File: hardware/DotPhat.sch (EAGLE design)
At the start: 32 parts, among them CN1 1X4-BIG, IC1 CAT24M010TS, J2 RASPBERRYPI-40-PIN-GPIO_PTH, J3 USB-MICROB, U1 ATMEGA328P-MU-QFN32, U2 TMP102, U3 ATSHA204-TSU, X3 S4B-ZR

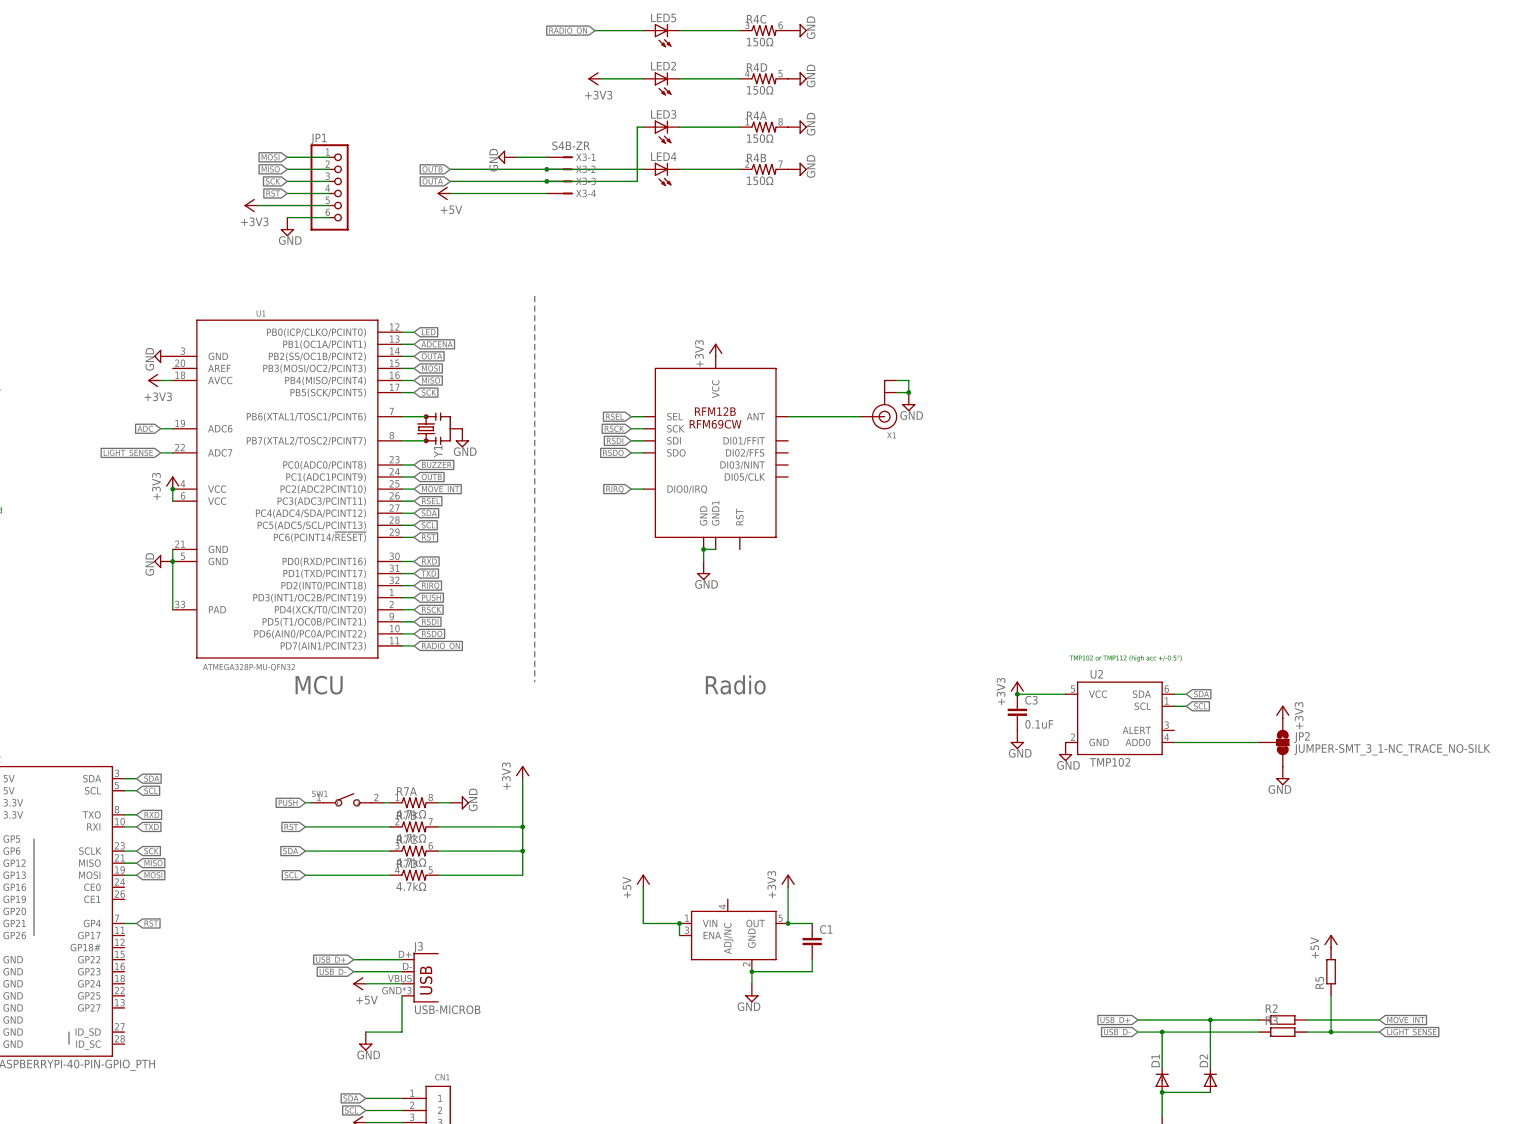
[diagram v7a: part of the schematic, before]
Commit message: Make USB_D+ and USB_D- part of the same port. Required for Micronucleus.
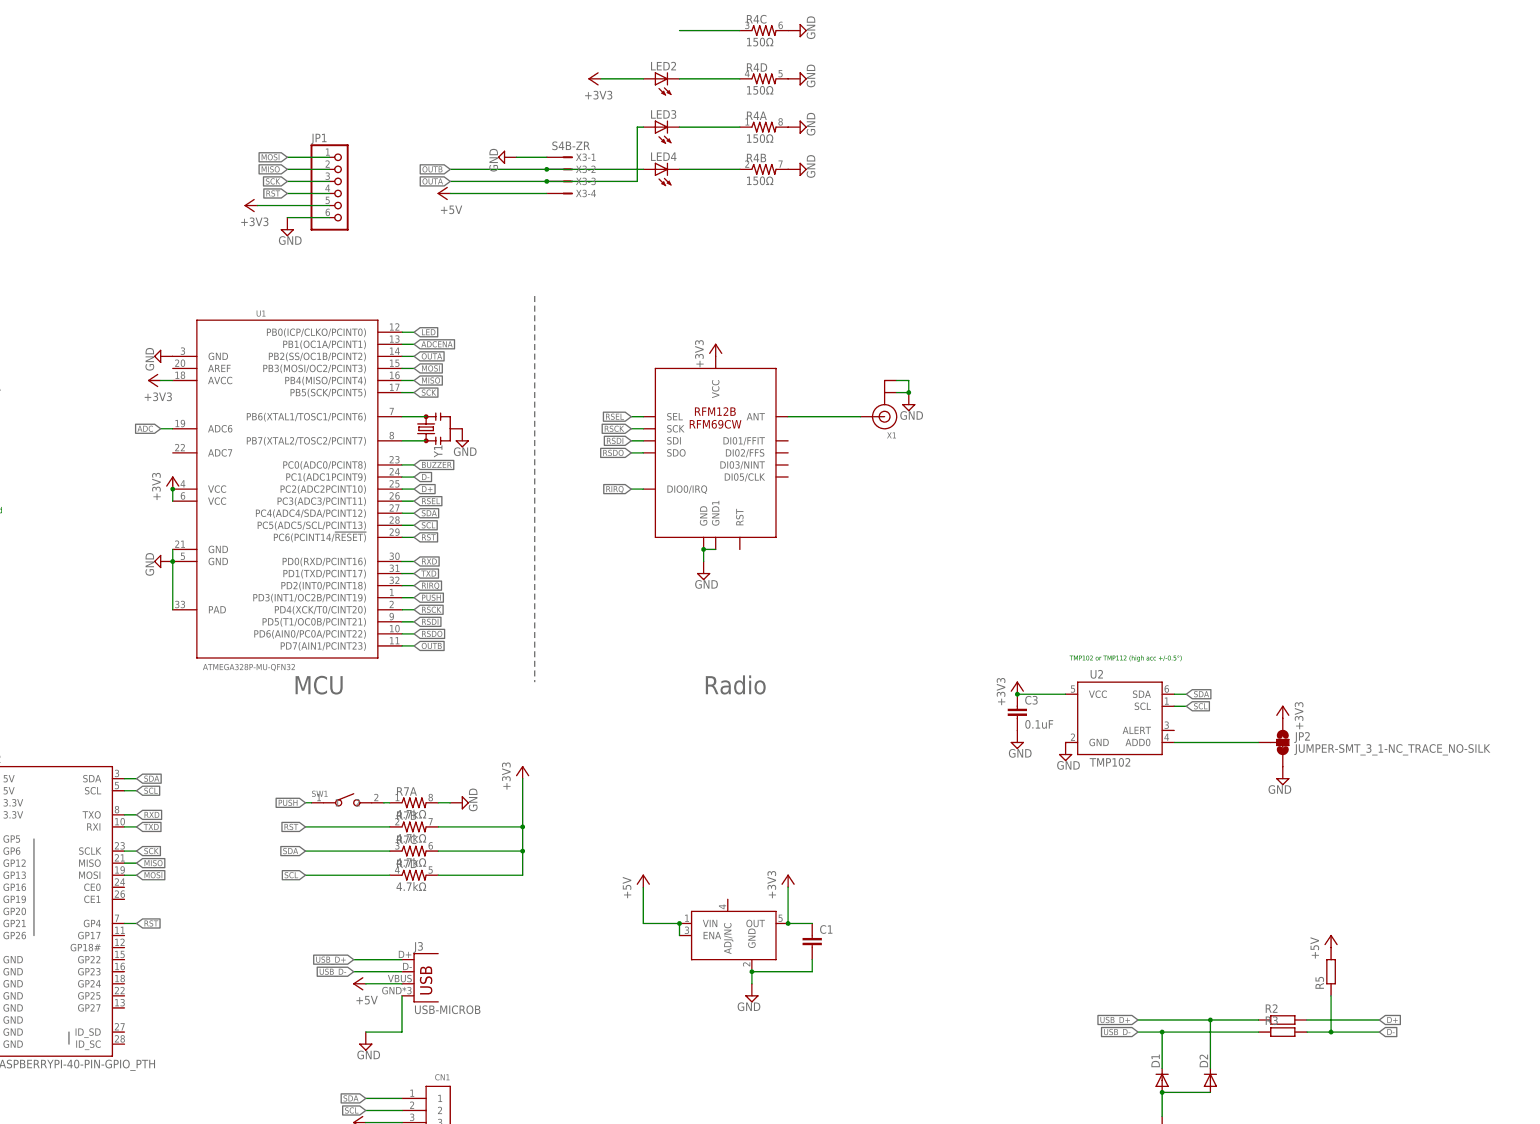
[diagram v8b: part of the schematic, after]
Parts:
- removed LED5: (no value), SparkFun:LED0603
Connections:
- net MOVE_INT renamed D+
- removed net LIGHT_SENSE: R3.2, R5.1, U1.ADC7
- removed net RADIO_ON: LED5.A, U1.PD7(AIN1/PCINT23)
- new net D-: R3.2, R5.1, U1.PC1(ADC1PCINT9)
- net N$10: no longer LED5.C
- net OUTB: now also U1.PD7(AIN1/PCINT23); no longer U1.PC1(ADC1PCINT9)
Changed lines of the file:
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@@
 <part name="+3V7" library="supply1" deviceset="+3V3" device=""/>
 <part name="R4" library="SparkFun" deviceset="RESISTOR-ARRAY" device="0603-ARV" value="150Ω"/>
-<part name="LED5" library="SparkFun" deviceset="LED" device="0603"/>
 <part name="SUPPLY12" library="supply2" deviceset="GND" device=""/>
 <part name="U$4" library="LDCL015" deviceset="LDCL015" device=""/>
@@
 <instance part="R4" gate="C" x="152.4" y="152.4"/>
 <instance part="R4" gate="D" x="152.4" y="142.24"/>
-<instance part="LED5" gate="G$1" x="129.54" y="152.4" rot="R90"/>
 <instance part="SUPPLY12" gate="GND" x="160.02" y="152.4" rot="R90"/>
 <instance part="U$4" gate="G$1" x="144.78" y="-38.1"/>
@@
 </segment>
 </net>
-<net name="LIGHT_SENSE" class="0">
-<segment>
-<pinref part="U1" gate="G$1" pin="ADC7"/>
-<wire x1="27.94" y1="63.5" x2="25.4" y2="63.5" width="0.1524" layer="91"/>
-<label x="25.4" y="63.5" size="1.27" layer="95" rot="R180" xref="yes"/>
-</segment>
-<segment>
-<pinref part="R3" gate="G$1" pin="2"/>
-<wire x1="266.7" y1="-58.42" x2="271.78" y2="-58.42" width="0.1524" layer="91"/>
-<pinref part="R5" gate="G$1" pin="1"/>
-<wire x1="271.78" y1="-58.42" x2="281.94" y2="-58.42" width="0.1524" layer="91"/>
-<wire x1="271.78" y1="-50.8" x2="271.78" y2="-58.42" width="0.1524" layer="91"/>
-<junction x="271.78" y="-58.42"/>
-<label x="281.94" y="-58.42" size="1.27" layer="95" xref="yes"/>
-</segment>
-</net>
 <net name="RSEL" class="0">
 <segment>
@@
 </segment>
 </net>
-<net name="MOVE_INT" class="0">
-<segment>
-<pinref part="U1" gate="G$1" pin="PC2(ADC2PCINT10)"/>
-<wire x1="76.2" y1="55.88" x2="78.74" y2="55.88" width="0.1524" layer="91"/>
-<label x="78.74" y="55.88" size="1.27" layer="95" xref="yes"/>
-</segment>
-<segment>
-<pinref part="R2" gate="G$1" pin="2"/>
-<wire x1="266.7" y1="-55.88" x2="281.94" y2="-55.88" width="0.1524" layer="91"/>
-<label x="281.94" y="-55.88" size="1.27" layer="95" xref="yes"/>
-</segment>
-</net>
 <net name="RXD" class="0">
 <segment>
@@
 </net>
 <net name="OUTB" class="0">
-<segment>
-<pinref part="U1" gate="G$1" pin="PC1(ADC1PCINT9)"/>
-<wire x1="76.2" y1="58.42" x2="78.74" y2="58.42" width="0.1524" layer="91"/>
-<label x="78.74" y="58.42" size="1.27" layer="95" xref="yes"/>
-</segment>
 <segment>
 <label x="86.36" y="123.19" size="1.27" layer="95" rot="R180" xref="yes"/>
@@
 <wire x1="106.68" y1="123.19" x2="127" y2="123.19" width="0.1524" layer="91"/>
 <junction x="106.68" y="123.19"/>
+</segment>
+<segment>
+<pinref part="U1" gate="G$1" pin="PD7(AIN1/PCINT23)"/>
+<wire x1="76.2" y1="22.86" x2="78.74" y2="22.86" width="0.1524" layer="91"/>
+<label x="78.74" y="22.86" size="1.27" layer="95" xref="yes"/>
 </segment>
 </net>
@@
 <segment>
 <pinref part="R4" gate="C" pin="1"/>
-<pinref part="LED5" gate="G$1" pin="C"/>
 <wire x1="147.32" y1="152.4" x2="134.62" y2="152.4" width="0.1524" layer="91"/>
-</segment>
-</net>
-<net name="RADIO_ON" class="0">
-<segment>
-<pinref part="LED5" gate="G$1" pin="A"/>
-<wire x1="127" y1="152.4" x2="116.84" y2="152.4" width="0.1524" layer="91"/>
-<label x="116.84" y="152.4" size="1.27" layer="95" rot="R180" xref="yes"/>
-</segment>
-<segment>
-<pinref part="U1" gate="G$1" pin="PD7(AIN1/PCINT23)"/>
-<wire x1="76.2" y1="22.86" x2="78.74" y2="22.86" width="0.1524" layer="91"/>
-<label x="78.74" y="22.86" size="1.27" layer="95" xref="yes"/>
 </segment>
 </net>
@@
 </segment>
 </net>
+<net name="D-" class="0">
+<segment>
+<pinref part="R3" gate="G$1" pin="2"/>
+<wire x1="266.7" y1="-58.42" x2="271.78" y2="-58.42" width="0.1524" layer="91"/>
+<pinref part="R5" gate="G$1" pin="1"/>
+<wire x1="271.78" y1="-58.42" x2="281.94" y2="-58.42" width="0.1524" layer="91"/>
+<wire x1="271.78" y1="-50.8" x2="271.78" y2="-58.42" width="0.1524" layer="91"/>
+<junction x="271.78" y="-58.42"/>
+<label x="281.94" y="-58.42" size="1.27" layer="95" xref="yes"/>
+</segment>
+<segment>
+<pinref part="U1" gate="G$1" pin="PC1(ADC1PCINT9)"/>
+<wire x1="76.2" y1="58.42" x2="78.74" y2="58.42" width="0.1524" layer="91"/>
+<label x="78.74" y="58.42" size="1.27" layer="95" xref="yes"/>
+</segment>
+</net>
+<net name="D+" class="0">
+<segment>
+<pinref part="U1" gate="G$1" pin="PC2(ADC2PCINT10)"/>
+<wire x1="76.2" y1="55.88" x2="78.74" y2="55.88" width="0.1524" layer="91"/>
+<label x="78.74" y="55.88" size="1.27" layer="95" xref="yes"/>
+</segment>
+<segment>
+<pinref part="R2" gate="G$1" pin="2"/>
+<wire x1="266.7" y1="-55.88" x2="281.94" y2="-55.88" width="0.1524" layer="91"/>
+<label x="281.94" y="-55.88" size="1.27" layer="95" xref="yes"/>
+</segment>
+</net>
